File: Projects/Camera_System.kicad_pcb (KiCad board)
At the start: 2 copper layers, 1 part, among them U1 IFX1117ME_V33

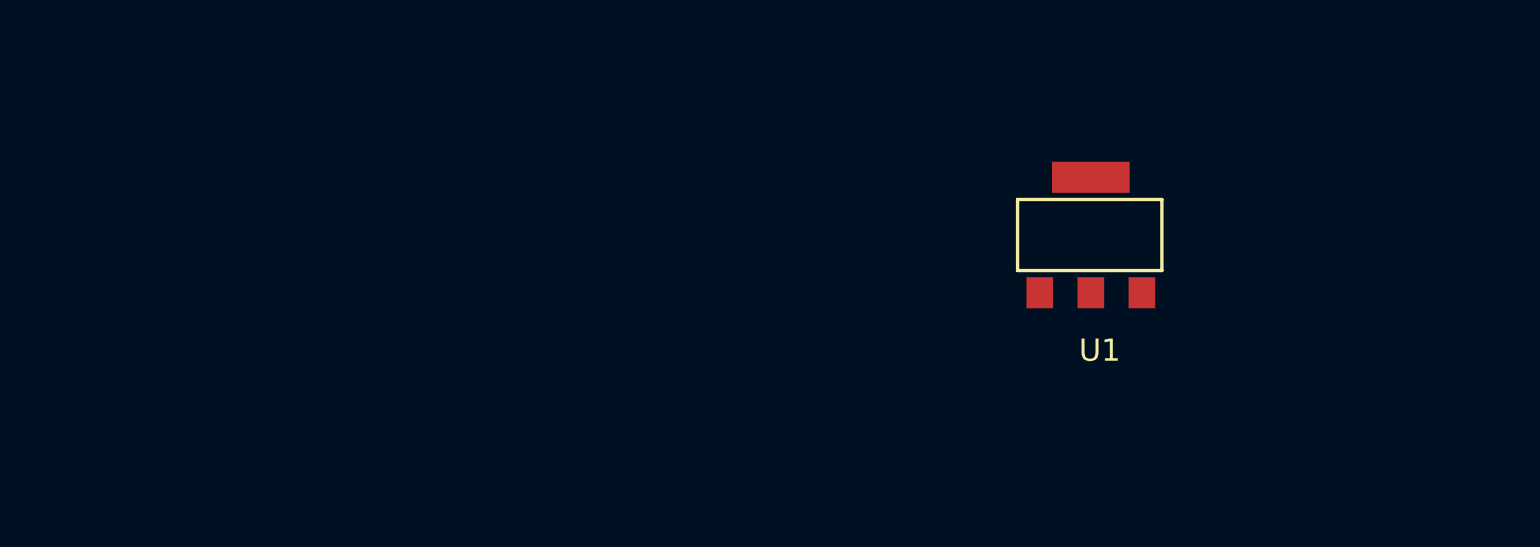
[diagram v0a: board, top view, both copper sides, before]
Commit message: Power Management Layout Created
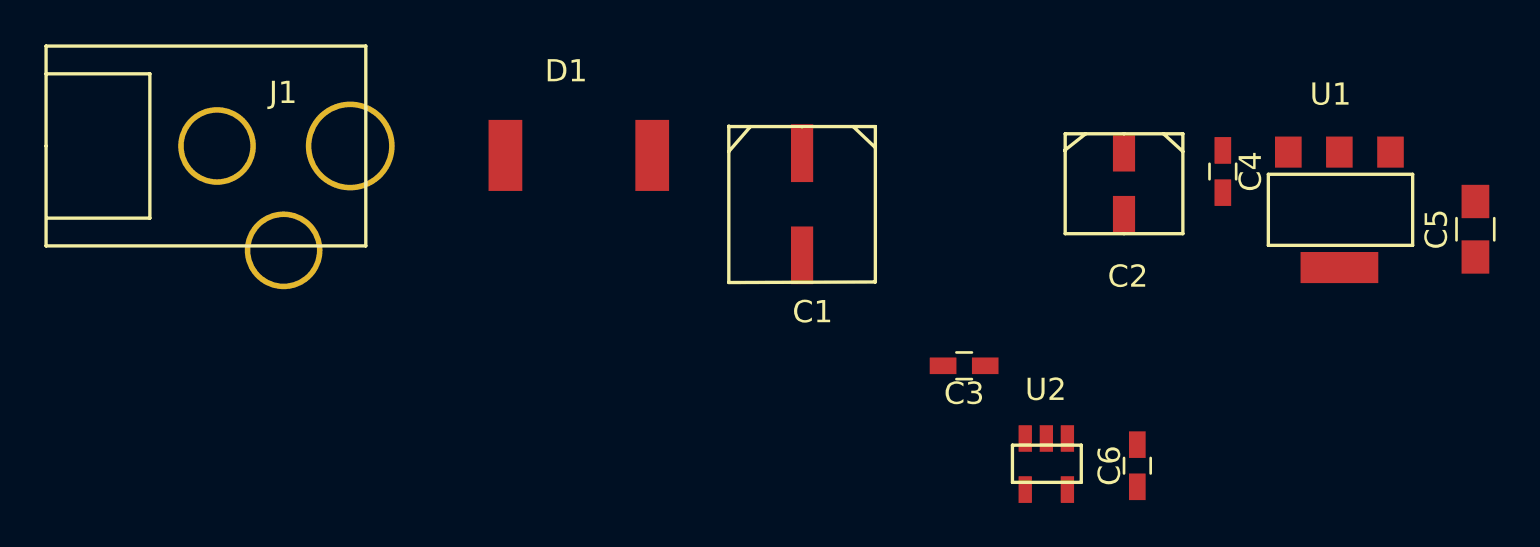
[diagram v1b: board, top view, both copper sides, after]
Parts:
- added C1: 47u, MyLibraries:UWT1E470MCL6GS, F.Cu at (138.1, 99.1)
- added C2: 10u, MyLibraries:UWX1E100MCL1GB, F.Cu at (152.6, 99.1)
- added C3: 1u, Capacitors_SMD:C_0603_HandSoldering, F.Cu at (145.4, 108.7)
- added C4: 100n, Capacitors_SMD:C_0603_HandSoldering, F.Cu at (157.1, 100.0)
- added C5: 22u, Capacitors_SMD:C_0805_HandSoldering, F.Cu at (168.4, 102.5)
- added C6: 2.2u, Capacitors_SMD:C_0603_HandSoldering, F.Cu at (153.2, 113.2)
- added D1: CS3M, MyLibraries:CS3M, F.Cu at (131.4, 99.2)
- added J1: BARREL_JACK, MyLibraries:PJ-002B, F.Cu at (114.8, 98.8)
- added U2: LD2980ABM50TR, MyLibraries:LD2980ABM50TR, F.Cu at (149.1, 112.0)
- moved U1 12.9 mm to (162.3, 99.1), turned to 180 degrees
